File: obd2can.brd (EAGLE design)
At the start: 96.5 x 87.9 mm, 109 parts, among them IC1 SCANTOOL, IC3 LM339PWR, IC4 MCP2551, Q10 BSS138, Q1000 8MHz, Q3 MMBT2222, Q4 MMBT2222, Q7 ZXMP6A13FTA, Q8 MMBT2222, Q9 BSS138, SW1 6X3.5_TACT, U1 3.3V, U1000 SN65HVD235DR, U2 V_REG_317DPACK, U2000 STM32F072-LQFP48, U3 5V Reg., U3000 AP3211KTR-G1, X1000 RJ45_RIGHT_ANGLEMOLEX_95001-2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, X2 Male DB9, X2000 RJ45_RIGHT_ANGLEMOLEX_95001-2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, Y1 16MHz

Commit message: label adjustment, snapshot image
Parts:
- removed C1000: 10uF, rcl:SMC_A
- removed C10000: 1uf, rcl:C0603K
- removed C11000, C13000: 22uF, rcl:C1206
- removed C2000, C6000, C9000: 0.1uf, rcl:C0603K
- removed C3000, C7000: 4.7uf, rcl:C0603K
- removed C4000: 0.01uf, rcl:C0603K
- removed D1000: (no value), diode:SMC
- removed D2000: 400V 1A, smt_diodes:SMA
- removed D3000: SCHOTTKY, smt_diodes:SMA
- removed IC3: LM339PWR, _stn_logic:TSSOP-14
- removed IC4: MCP2551, _stn_microchip:SO-8
- removed JP1: (no value), SparkFun:1X08
- removed JP8: DNP, SparkFun:FTDI_BASIC
- removed JP9: DNP, SparkFun:1X02
- removed L1000: (no value), wuerth-elektronik:1812
- removed L2000: 4.7uH, rcl:L2012C
- removed LED4, LED5: RED, SparkFun:LED-0603
- removed Q10, Q9: BSS138, SparkFun:SOT23-3
- removed Q1000: 8MHz, SparkFun2:CRYSTAL-SMD-5X3
- removed Q8: MMBT2222, SparkFun:SOT23-3
- removed R1000: 120, rcl:R0603
- removed R3000: 49.9K 1%, rcl:R0603
- removed R33: 10k, SparkFun:0402-RES
- removed R34: 1.5k, SparkFun:0402-RES
- removed R35, R37: 330, SparkFun:0402-RES
- removed R4000: 16.2K 1%, rcl:R0603
- removed R5000: 4.7K, rcl:R0603
- removed SV1000: (no value), con-lstb:MA06-1
- removed TC1000: TC2030-IDC-NL, TagConnect:TC2030-IDC-NL
- removed U1000: SN65HVD235DR, can:SO08
- removed U2000: STM32F072-LQFP48, stm32f0:LQFP48
- removed U3000: AP3211KTR-G1, diodes_inc:SOT-23-6
- removed X1000, X2000: RJ45_RIGHT_ANGLEMOLEX_95001-2881, FCI_RJ12:RJ45_RIGHT_ANGLE_MOLEX_95001-2881
- added C20, C23: 10uF, SparkFun:EIA3216
- added C21: 2.2uF, SparkFun:0402-CAP
- added C22: 470pF, SparkFun:0402-CAP
- added C24: 0.1uF, SparkFun:0402-CAP
- added D5: 400V 1A, smt_diodes:SMA
- added D6: SCHOTTKY, smt_diodes:SMA
- added IC2: SCANTOOL, SparkFun:_STN_SCANTOOL_QFN-28-S
- added L1: (no value), wuerth-elektronik:1812
- added L2: 4.7uH, rcl:L2012C
- added Q1: BSS138, SparkFun:SOT23-3
- added Q2, Q5, Q6: MMBT2222, SparkFun:SOT23-3
- added SV1: (no value), con-lstb:MA06-1
- added TC1: TC2030-IDC-NL, TagConnect:TC2030-IDC-NL
- added U4: STM32F072-LQFP48, stm32f0:LQFP48
- added U5: 5V Reg., SparkFun:SOT23-5
- added X1: RJ45_RIGHT_ANGLEMOLEX_95001-2881, FCI_RJ12:RJ45_RIGHT_ANGLE_MOLEX_95001-2881
- C1, C6: value 1uF -> 0.1uF
- C10: value 0.1uF -> 0.1uf; device SparkFun:0402-CAP -> rcl:C0603K
- C11: value 1uF -> 10uF; device SparkFun:0402-CAP -> rcl:SMC_A
- C12: value 560pF -> 4.7uf; device SparkFun:0402-CAP -> rcl:C0603K
- C13: value 560pF -> 0.01uf; device SparkFun:0402-CAP -> rcl:C0603K
- C14: value 0.1uF -> 22uF; device SparkFun:0402-CAP -> rcl:C1206
- C15: value 2.2uF -> 10nF; device SparkFun:0402-CAP -> rcl:C0603
- C16: value 470pF -> 0.1uf; device SparkFun:0402-CAP -> rcl:C0603K
- C17: value 1uF -> 4.7uf; device SparkFun:0402-CAP -> rcl:C0603K
- C18: value 10uF -> 22uF; device SparkFun:EIA3216 -> rcl:C1206
- C19: value 10nF -> 1uf; device rcl:C0603 -> rcl:C0603K
- C2: value 27pF -> 1uF
- C7: value 0.1uF -> 27pF
- C8: value 4.7uF -> 1uF
- C9: value 10uF -> 0.1uf; device SparkFun:EIA3216 -> rcl:C0603K
- D4: value MBRA140 -> (none); device SparkFun:SMA-DIODE -> diode:SMC
- IC1: value SCANTOOL -> LM339PWR; device SparkFun:_STN_SCANTOOL_QFN-28-S -> _stn_logic:TSSOP-14
- LED3: value YELLOW -> RED
- Q3: value MMBT2222 -> ZXMP6A13FTA; device SparkFun:SOT23-3 -> SparkFun:SOT23
- Q4: value MMBT2222 -> BSS138
- Q7: value ZXMP6A13FTA -> 8MHz; device SparkFun:SOT23 -> SparkFun2:CRYSTAL-SMD-5X3
- R1: value 10k -> 10K
- R10: value 10k -> 374
- R11: value 510 0.5W -> 330; device _stn_rcl:2010 -> SparkFun:0402-RES
- R13: value 1k -> 1.2k
- R14: value 100 -> 866
- R15: value 100 -> 10k
- R16: value 4.7k -> 240
- R17: value 1.2k -> 10k
- R19: value 866 -> 10k
- R2: value 1k -> 62K
- R20: value 240 -> 120; device SparkFun:0402-RES -> rcl:R0603
- R21, R27, R28, R9: value 10k -> 1k
- R22: value 374 -> 10k
- R23: value 4.7k -> 10k
- R25: value 4.7k -> 4.7K; device SparkFun:0402-RES -> rcl:R0603
- R26: value 4.7K -> 510 0.5W; device rcl:R0603 -> _stn_rcl:2010
- R29: value 10k -> 49.9K 1%; device SparkFun:0402-RES -> rcl:R0603
- R3: value 62K -> 10k
- R30: value 10k -> 16.2K 1%; device SparkFun:0402-RES -> rcl:R0603
- R31: value 10k -> 4.7K; device SparkFun:0402-RES -> rcl:R0603
- R32: value 1k -> 510 0.5W; device SparkFun:0402-RES -> _stn_rcl:2010
- R4, R5: value 330 -> 10k
- R6: value 10K -> 10k
- R7: value 1k -> 330
- R8: value 510 0.5W -> 4.7k; device _stn_rcl:2010 -> SparkFun:0402-RES
- U1: value 3.3V -> V_REG_317DPACK; device SparkFun:SOT23-5 -> SparkFun:V-REG_DPACK
- U2: value V_REG_317DPACK -> SN65HVD235DR; device SparkFun:V-REG_DPACK -> can:SO08
- U3: value 5V Reg. -> AP3211KTR-G1; device SparkFun:SOT23-5 -> diodes_inc:SOT-23-6
- X2: value Male DB9 -> RJ45_RIGHT_ANGLEMOLEX_95001-2881; device SparkFun:DB9_MALE -> FCI_RJ12:RJ45_RIGHT_ANGLE_MOLEX_95001-2881
- moved R26 80.0 mm to (78.5, 20.1), turned to 0 degrees
- moved C5 67.8 mm to (78.5, 27.7), turned to 0 degrees
- moved X2 62.3 mm to (92.7, 14.0), turned to 90 degrees
- moved C19 57.0 mm to (46.7, 2.29)
- moved R22 54.0 mm to (59.7, 25.9), turned to 90 degrees
- moved R19 53.5 mm to (59.7, 28.4)
- moved LED2 50.8 mm to (73.4, 31.5), turned to 180 degrees
- moved R10 50.3 mm to (78.5, 31.5)
- moved SW1 47.3 mm to (29.7, 6.86)
- moved IC1 47.2 mm to (58.4, 32.3), turned to 270 degrees
- moved R27 45.8 mm to (75.9, 16.3), turned to 270 degrees
- moved R5 45.7 mm to (63.5, 34.8), turned to 0 degrees
- moved R9 45.6 mm to (74.7, 31.5), turned to 270 degrees
- moved R32 45.6 mm to (78.5, 8.64), turned to 0 degrees
- moved R6 44.8 mm to (52.1, 33.5), turned to 0 degrees
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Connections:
- removed net 3.3V: C1.1, C5.1, C8.1, IC1.10, IC1.25, LED1.A, LED2.A, LED3.A, LED4.A, R18.2, R27.2, R9.2, U1.5
- removed net CAN_HI: IC4.7, JP1.6, R14.2, X2.3
- removed net CAN_LO: IC4.6, JP1.7, R15.2, X2.5
- removed net N$10: C12.1, R14.1
- removed net N$11: IC4.8, R16.2
- removed net N$27: C13.1, R15.1
- removed net N$35: LED1.C, R35.2
- removed net N$36: LED2.C, R37.1
- removed net RX-I: IC1.13, JP8.TXO
- removed net RX-STAT: IC1.21, R35.1
- removed net TX-O: IC1.14, JP8.RXI, R25.2
- removed net TX-STAT: IC1.20, R37.2
- removed net USART2_RX: U2000.13
- removed net USART2_TX: U2000.12
- removed net VBAT: C14.1, D4.C, IC3.3, JP1.8, R10.1, R11.1, R8.1, U2.3
- removed net VBATT_RAW: D4.A, R3.2, X2.9
- new net RESET_STN: IC2.26
- new net RX_FROM_STN: IC2.14, U4.13
- new net TX_TO_STN: IC2.13, U4.12
- net !ISO_K_TX: now also IC2.22, R28.2; no longer IC1.22, R13.2
- net !ISO_L_TX: now also IC2.23, R27.2; no longer IC1.23, R7.2
- net !ISO_RX: now also IC1.2, IC2.8, R4.1; no longer IC1.8, IC3.2, R9.1
- net !OBD_RX_STATUS!/PGC: now also IC2.19, R7.1; no longer IC1.19, R4.1
- net !PWR_SAVE: now also IC2.15; no longer IC1.15
- net !VPW_RX: now also IC1.14, IC2.1, R5.1; no longer IC1.1, IC3.14, R18.1
- net +12V: now also L1.2, R2.2, X1.P8, X2.P8; no longer L1000.2, X1000.P8, X2000.P8
- net +5V: now also SV1.3; no longer SV1000.3
- net 5V: now also C20.A, C21.1, D1.2, R13.2, U5.5; no longer C11.1, C15.1, C18.A, C6.1, D3.2, IC4.3, R1.2, R17.2, R25.1, R34.1, U1.1, U1.3, U3.5
- net AGND: now also U4.8; no longer U2000.8
- net ANALOG_1_ADC: now also U4.10; no longer U2000.10
- net BATT_V: now also C1.1, IC2.27, R1.2, R2.1; no longer C7.1, IC1.27, R3.1, R6.2
- net CANH: now also R20.1, U2.7, X1.P2; no longer R1000.1, U1000.7, X1000.P2
- net CANL: now also R20.2, U2.6, X1.P3; no longer R1000.2, U1000.6, X1000.P3
- net CAN_RX: now also U2.4, U4.32; no longer IC1.11, IC4.4, U1000.4, U2000.32
- net CAN_TX: now also U2.1, U4.33; no longer IC1.12, IC4.1, R34.2, U1000.1, U2000.33
- net GND: now also C11.-, C18.2, C19.2, C20.C, C21.2, C22.2, C23.C, C24.2, C9.2, D4.A, D6.A, IC1.12, IC2.16, IC2.24, IC2.5, IC2.EXP, LED2.C, Q1.2, Q2.2, Q5.2, Q6.2, R1.1, R10.1, R15.2, R25.1, R30.2, R8.1, SV1.1, TC1.5, U2.2, U2.5, U4.23, U4.35, U4.44, U4.47, U5.2, X1.P1, X2.P1; no longer C1000.-, C10000.2, C11.2, C11000.2, C13000.2, C15.2, C18.C, C2000.2, C3000.2, C4000.2, C6000.2, C7000.2, C9.C, C9000.2, D1000.A, D3000.A, IC1.16, IC1.24, IC1.5, IC1.EXP, IC3.12, IC4.2, JP1.1, JP8.GND, JP9.2, LED5.C, Q10.2, Q3.2, Q8.2, Q9.2, R16.1, R22.1, R23.1, R26.1, R33.2, R4000.2, R6.1, SV1000.1, TC1000.5, U1.2, U1000.2, U1000.5, U2000.23, U2000.35, U2000.44, U2000.47, U3000.2, X1000.P1, X2.1, X2.2, X2000.P1
- net HOST_PRESENT: now also IC2.9; no longer IC1.9
- net J1850BUS+: now also D3.1, R18.1, R19.1, R23.1, X2.P4; no longer D1.1, JP1.3, R21.1, R28.1, R30.1, X2.7
- net J1850BUS+_TX: now also IC2.3, Q4.1; no longer IC1.3, Q9.1
- net J1850BUS-: now also Q2.3, R17.1, R22.2, X2.P5; no longer JP1.2, Q8.3, R29.1, R31.2, X2.6
- net J1850BUS-_TX: now also IC2.4, R21.1; no longer IC1.4, R32.1
- net K-LINE: now also Q6.3, R32.2, R6.1, X2.P7; no longer JP1.5, Q4.3, R11.2, R12.1, X2.4
- net L-LINE: now also Q5.3, R26.2, X2.P6; no longer JP1.4, Q3.3, R8.2, X2.8
- net N$1: now also IC1.7, R18.2; no longer IC3.7, R28.2
- net N$12: now also IC1.9, R13.1, R8.2; no longer IC3.9, R17.1, R23.2
- net N$13: now also IC1.4, R6.2; no longer IC3.4, R12.2
- net N$14: now also D1.1, R22.1; no longer D3.1, R31.1
- net N$15: now also R25.2, U2.8; no longer R26.2, U1000.8
- net N$16: now also R29.2, R30.1, U3.3; no longer R3000.2, R4000.1, U3000.3
- net N$17: now also C15.2, U3.1; no longer C19.2, U3000.1
- net N$18: now also Q3.1, Q4.3; no longer Q7.1, Q9.3
- net N$19: now also C15.1, D6.C, L2.1, U3.6; no longer C19.1, D3000.C, L2000.1, U3000.6
- net N$22: now also Q1.3, R10.2, R14.1; no longer Q10.3, R19.1, R22.2
- net N$24: now also R23.2; no longer R30.2
- net N$25: now also Q2.1, R21.2; no longer Q8.1, R32.2
- net N$26: now also IC2.17; no longer IC1.17
- net N$3: now also IC1.6, R17.2; no longer IC3.6, R29.2
- net N$30: now also LED1.C, R7.2; no longer LED3.C, R4.2
- net N$31: now also LED3.C, R11.1; no longer LED4.C, R5.1
- net N$32: now also LED2.A, R9.1; no longer LED5.A, R2.1
- net N$34: now also C22.1, U5.4; no longer C16.1, U3.4
- net N$4: now also Q6.1, R28.1; no longer Q4.1, R13.1
- net N$40: now also Q7.3, U4.6; no longer Q1000.3, U2000.6
- net N$42: now also Q7.1, U4.5; no longer Q1000.1, U2000.5
- net N$5: now also Q5.1, R27.1; no longer Q3.1, R7.1
- net N$50: now also D5.A, L1.1; no longer D2000.A, L1000.1
- net N$6: now also IC1.5, R12.2, R15.1; no longer IC3.5, R10.2, R33.1
- net N$7: now also IC1.8, R19.2; no longer IC3.8, R21.2
- net N$8: now also R14.2, R16.2, U1.1; no longer R19.2, R20.2, U2.1
- net N$9: now also D3.2, Q3.3; no longer D1.2, Q7.3
- net OSC1: now also C3.1, IC2.6; no longer C2.1, IC1.6
- net OSC2: now also C7.1, IC2.7; no longer C3.1, IC1.7
- net PWM/!VPW: now also IC2.28, Q1.1; no longer IC1.28, Q10.1
- net PWM_RX: now also IC1.1, IC2.2, R3.1; no longer IC1.2, IC3.1, R27.1
- net RESET: now also R31.1, TC1.3, U4.7; no longer IC1.26, R1.1, R5000.1, TC1000.3, U2000.7
- net RST_NVM: now also IC2.18, R11.2; no longer IC1.18, JP9.1, R5.2
- net SAFE12V: now also C14.1, C6.1, D4.C, D5.C, IC1.3, R12.1, R26.1, R32.1, U1.3, U3.4, U3.5; no longer C11000.1, D1000.C, D2000.C, U3000.4, U3000.5
- net SWCLK: now also TC1.4, U4.37; no longer TC1000.4, U2000.37
- net SWDIO: now also TC1.2, U4.34; no longer TC1000.2, U2000.34
- net U3: now also R29.1, R31.2, TC1.1; no longer R3000.1, R5000.2, TC1000.1
- net USART1_RX: now also SV1.4, U4.31; no longer SV1000.4, U2000.31
- net USART1_TX: now also SV1.5, U4.30; no longer SV1000.5, U2000.30
- net V+: now also C10.1, C11.+, C12.1, C13.1, C16.1, C17.1, C18.1, C19.1, C2.1, C8.1, C9.1, IC2.10, IC2.25, L2.2, LED1.A, LED3.A, R3.2, R4.2, R5.2, U2.3, U4.1, U4.24, U4.36, U4.48, U4.9; no longer C1000.+, C10000.1, C13000.1, C2000.1, C3000.1, C4000.1, C6000.1, C7000.1, C9000.1, L2000.2, U1000.3, U2000.1, U2000.24, U2000.36, U2000.48, U2000.9
- net VCC: now also C23.A, C24.1, C5.1, Q3.2, R16.1, R9.2, U1.4, U5.1, U5.3; no longer C10.1, C17.1, C9.A, Q7.2, R2.2, R20.1, U2.4, U3.1, U3.3
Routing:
- net 3.3V: track 98.1 -> 0.00 mm, vias 6 -> 0
- net 5V: track 124.3 -> 31.7 mm, vias 6 -> 2
- net VBAT: track 90.1 -> 0.00 mm, vias 8 -> 0
- net VCC: track 129.3 -> 63.2 mm, vias 22 -> 21
- net V+: track 2.29 -> 67.9 mm, vias 0 -> 5
- net K-LINE: track 67.2 -> 11.4 mm
- net SAFE12V: track 0.00 -> 51.1 mm, vias 0 -> 7
- net CAN_RX: track 42.5 -> 0.36 mm, vias 2 -> 0
- net CAN_LO: track 41.3 -> 0.00 mm
- net CAN_TX: track 39.3 -> 0.00 mm, vias 2 -> 0
- net CAN_HI: track 38.4 -> 0.00 mm
- net L-LINE: track 39.2 -> 4.29 mm
- net VBATT_RAW: track 29.2 -> 0.00 mm, vias 1 -> 0
- net J1850BUS+: track 47.7 -> 19.1 mm
- net J1850BUS-: track 41.7 -> 13.8 mm
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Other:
- board size 96.5 x 87.9 mm -> 96.5 x 40.6 mm
- board text removed: "+"
- board text removed: "-"
- board text removed: "10/13/10"
- board text removed: "BLK"
- board text removed: "CAN"
- board text removed: "GRN"
- board text removed: "HI"
- board text removed: "J1850"
- board text removed: "K"
- board text removed: "L"
- board text removed: "LINE"
- board text removed: "LO"
- board text removed: "NC"
- board text removed: "OBD-II-UART"
- board text removed: "OBDRX"
- board text removed: "OBDTX"
- board text removed: "POWER"
- board text removed: "RST_NVM"
- board text removed: "RX"
- board text removed: "RX-I"
- board text removed: "TX"
- board text removed: "TX-O"
- board text removed: "VBAT"

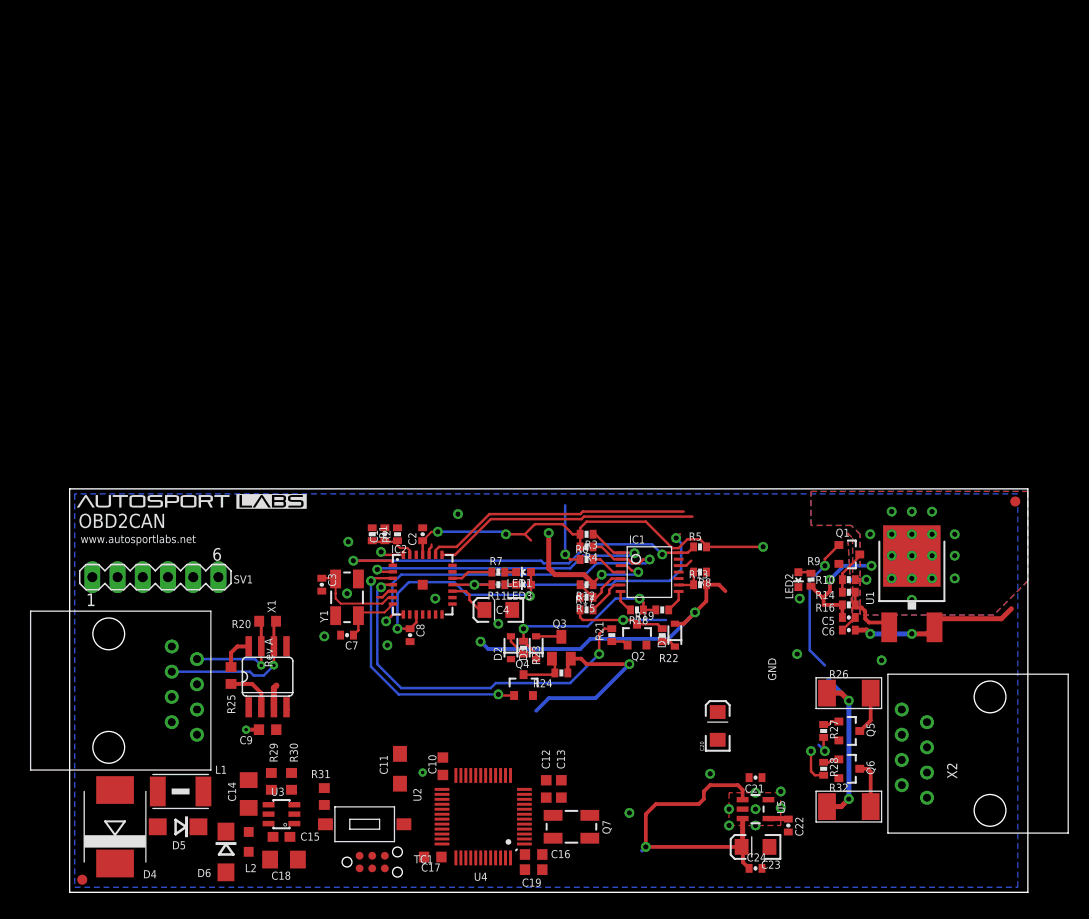
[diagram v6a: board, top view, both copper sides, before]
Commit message: OBD2CAN WIP - more air wires routed
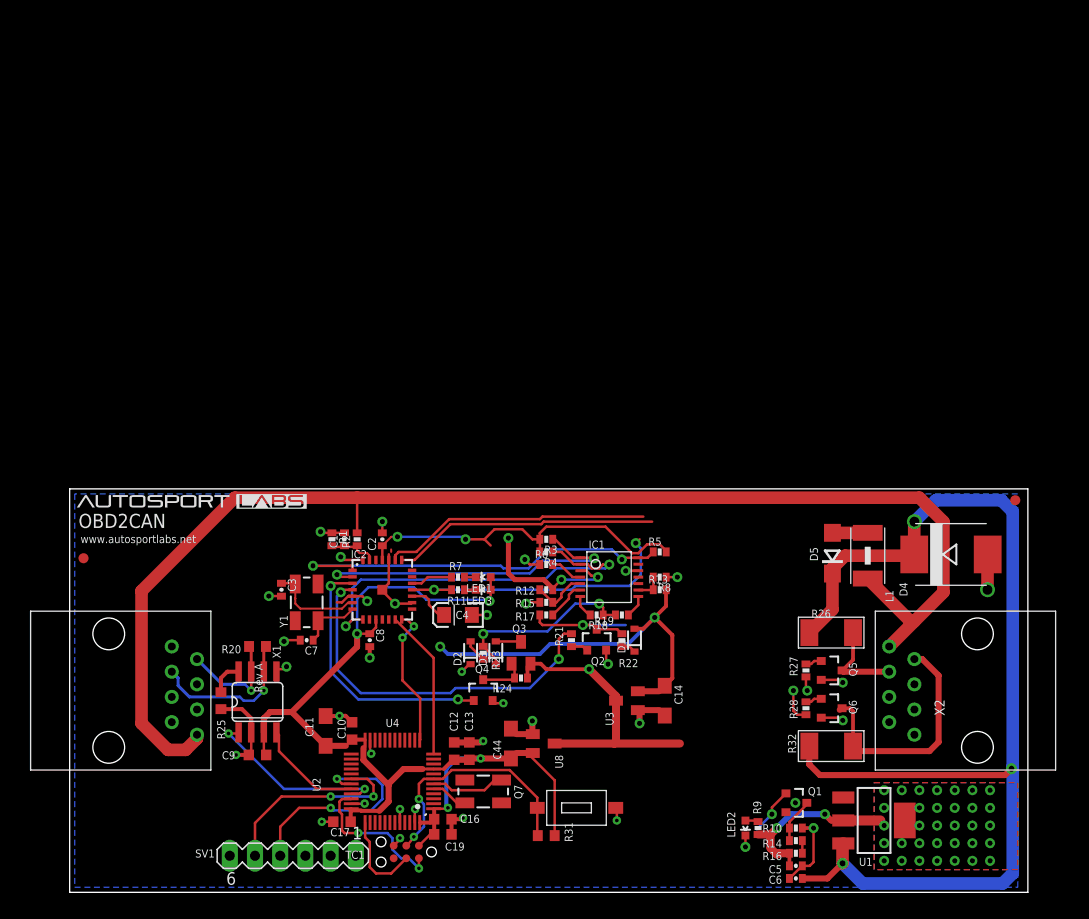
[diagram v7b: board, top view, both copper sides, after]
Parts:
- removed C15: 10nF, rcl:C0603
- removed C18: 22uF, rcl:C1206
- removed C20, C23: 10uF, SparkFun:EIA3216
- removed C21: 2.2uF, SparkFun:0402-CAP
- removed C22: 470pF, SparkFun:0402-CAP
- removed C24: 0.1uF, SparkFun:0402-CAP
- removed D6: SCHOTTKY, smt_diodes:SMA
- removed L2: 4.7uH, rcl:L2012C
- removed R29: 49.9K 1%, rcl:R0603
- removed R30: 16.2K 1%, rcl:R0603
- removed U5: 5V Reg., SparkFun:SOT23-5
- added C44: 10uF, rcl:SMC_A
- added U8: MCP1700-3.3, mcp1700:SOT-23
- C14: value 22uF -> 10uF; device rcl:C1206 -> rcl:SMC_A
- U1: value V_REG_317DPACK -> V_REG_317SMD; device SparkFun:V-REG_DPACK -> SparkFun:SOT223
- U3: value AP3211KTR-G1 -> MCP1700-5.0; device diodes_inc:SOT-23-6 -> mcp1700:SOT-23
- moved D4 88.6 mm to (88.8, 34.0), turned to 0 degrees
- moved L1 73.2 mm to (80.4, 33.9), turned to 270 degrees
- moved D5 71.4 mm to (76.8, 34.2), turned to 90 degrees
- moved C14 43.0 mm to (59.9, 19.3), turned to 270 degrees
- moved U3 36.6 mm to (56.1, 19.3)
- moved SV1 31.3 mm to (22.5, 3.68), turned to 180 degrees
- moved C6 25.6 mm to (73.2, 1.40)
- moved Q1 25.6 mm to (73.2, 9.02)
- moved C5 25.6 mm to (73.2, 2.67)
- moved LED2 25.6 mm to (68.1, 6.48)
- moved R10 25.6 mm to (73.2, 6.48)
- moved R14 25.6 mm to (73.2, 5.21)
- moved R16 25.6 mm to (73.2, 3.94)
- moved R9 25.6 mm to (69.3, 6.48)
- moved U1 24.6 mm to (81.0, 7.24), turned to 270 degrees
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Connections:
- removed net N$16: R29.2, R30.1, U3.3
- removed net N$17: C15.2, U3.1
- removed net N$19: C15.1, D6.C, L2.1, U3.6
- removed net N$34: C22.1, U5.4
- removed net U3: R29.1, R31.2, TC1.1
- net 5V: now also C14.+, U3.2; no longer C20.A, C21.1, U5.5
- net GND: now also C14.-, C44.-, U3.1, U8.1; no longer C14.2, C18.2, C20.C, C21.2, C22.2, C23.C, C24.2, D6.A, R30.2, U3.2, U5.2
- net SAFE12V: no longer C14.1, U3.4, U3.5
- net V+: now also C44.+, R31.2, TC1.1, U8.2; no longer C18.1, L2.2
- net VCC: now also U1.2, U3.3, U8.3; no longer C23.A, C24.1, U1.4, U5.1, U5.3
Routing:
- net +12V: track 0.00 -> 131.4 mm
- net SAFE12V: track 51.1 -> 131.8 mm, vias 7 -> 6
- net V+: track 67.9 -> 139.9 mm, vias 5 -> 6
- net GND: track 15.6 -> 80.8 mm, vias 22 -> 34
- net RESET: track 0.00 -> 24.9 mm, vias 0 -> 2
- net USART1_RX: track 0.00 -> 22.5 mm, vias 0 -> 2
- net USART1_TX: track 0.00 -> 20.0 mm, vias 0 -> 2
- net CAN_TX: track 0.00 -> 18.6 mm, vias 0 -> 2
- net VCC: track 63.2 -> 47.3 mm, vias 21 -> 36
- net SWDIO: track 0.00 -> 15.3 mm, vias 0 -> 2
- net TX_TO_STN: track 0.00 -> 15.2 mm
- net K-LINE: track 11.4 -> 25.8 mm
- net RX_FROM_STN: track 0.00 -> 14.2 mm, vias 0 -> 2
- net CAN_RX: track 0.36 -> 10.8 mm
- net SWCLK: track 0.00 -> 9.26 mm
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- removed copper zone on layer 1, net GND
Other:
- board text removed: "GND"

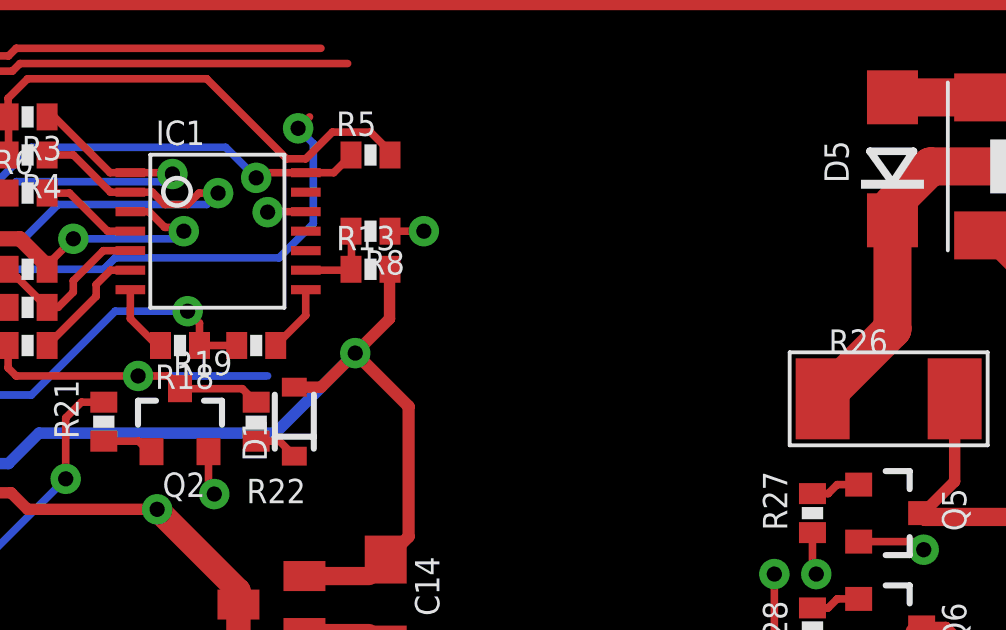
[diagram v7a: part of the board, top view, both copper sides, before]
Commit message: OBD2CAN WIP - more air wires routed
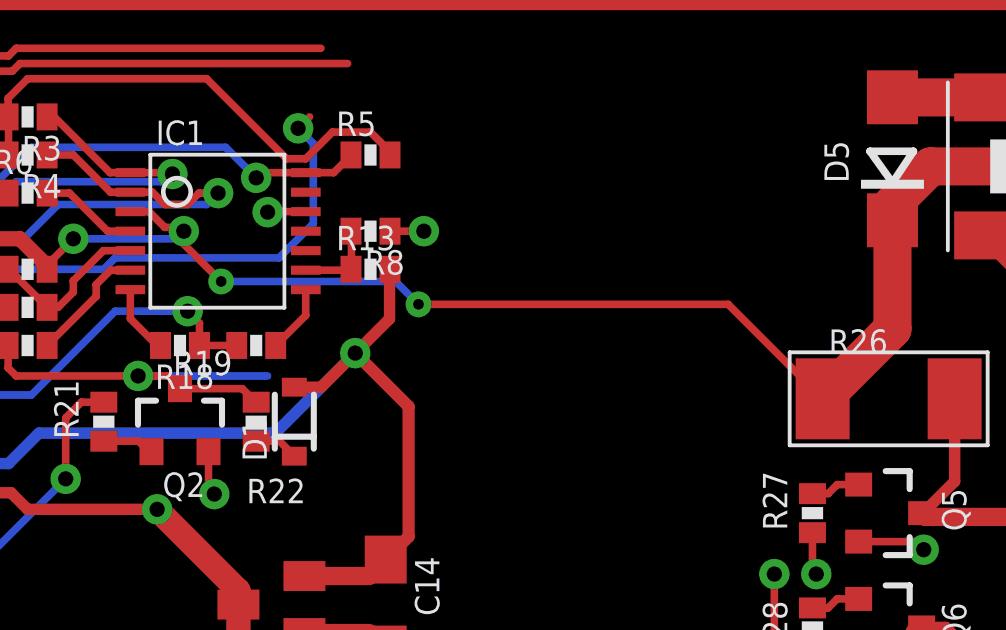
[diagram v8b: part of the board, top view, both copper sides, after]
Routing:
- net SAFE12V: track 131.8 -> 155.7 mm, vias 6 -> 8
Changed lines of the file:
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@@
 <wire x1="77.851" y1="2.921" x2="76.327" y2="1.397" width="0.6096" layer="1"/>
 <wire x1="76.327" y1="1.397" x2="73.802" y2="1.397" width="0.6096" layer="1"/>
-<wire x1="74.508" y1="26.162" x2="53.213" y2="31.75" width="0" layer="19" extent="1-1"/>
+<wire x1="74.508" y1="26.162" x2="71.3584" y2="29.3116" width="0.254" layer="1"/>
+<wire x1="71.3584" y1="29.3116" x2="61.0362" y2="29.3116" width="0.254" layer="1"/>
+<via x="61.0362" y="29.3116" extent="1-16" drill="0.3556"/>
+<wire x1="61.0362" y1="29.3116" x2="60.2742" y2="30.0736" width="0.254" layer="16"/>
+<wire x1="60.2742" y1="30.0736" x2="54.4576" y2="30.0736" width="0.254" layer="16"/>
+<via x="54.4576" y="30.0736" extent="1-16" drill="0.3556"/>
+<wire x1="54.4576" y1="30.0736" x2="53.213" y2="31.3182" width="0.254" layer="1"/>
+<wire x1="53.213" y1="31.3182" x2="53.213" y2="31.75" width="0.254" layer="1"/>
 </signal>
 <signal name="+12V">
